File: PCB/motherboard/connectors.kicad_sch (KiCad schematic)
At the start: 9 parts, among them J1 Conn_01x04, J2 Conn_01x08, J3 Conn_01x06, J4 Conn_01x03, J5 Conn_01x03, J6 Conn_01x02, J7 Screw_Terminal_01x03, J8 Screw_Terminal_01x09, J9 Conn_01x11

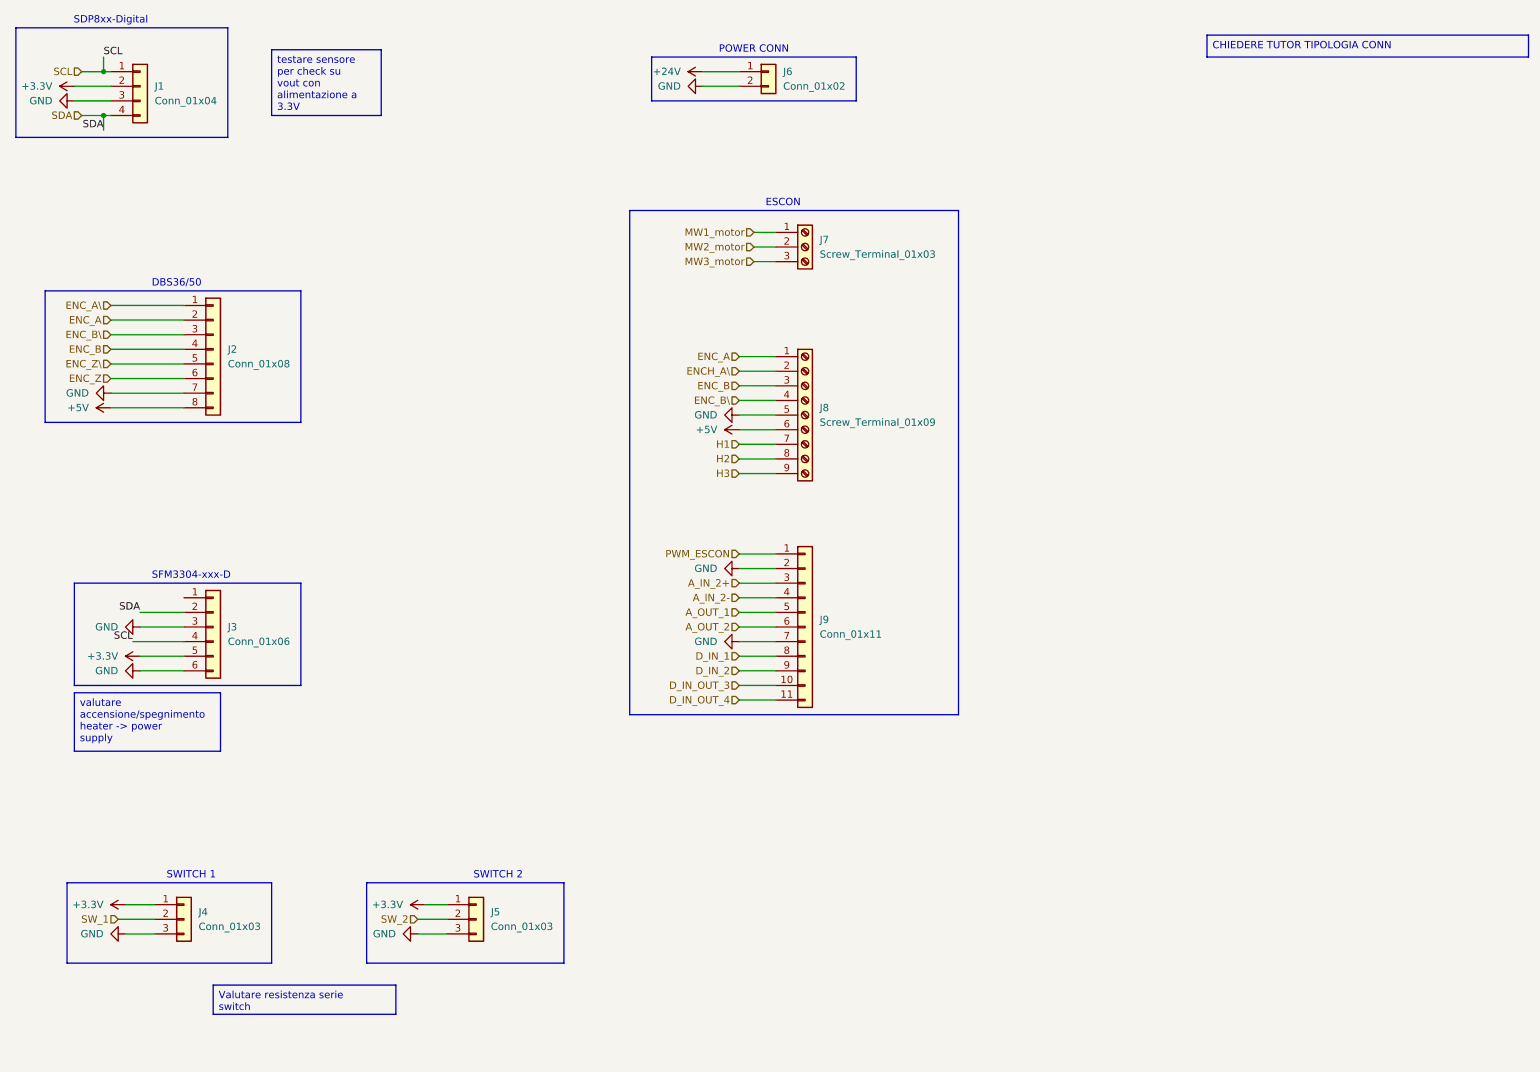
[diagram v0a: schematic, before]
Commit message: reverse current protection on ESCON+others
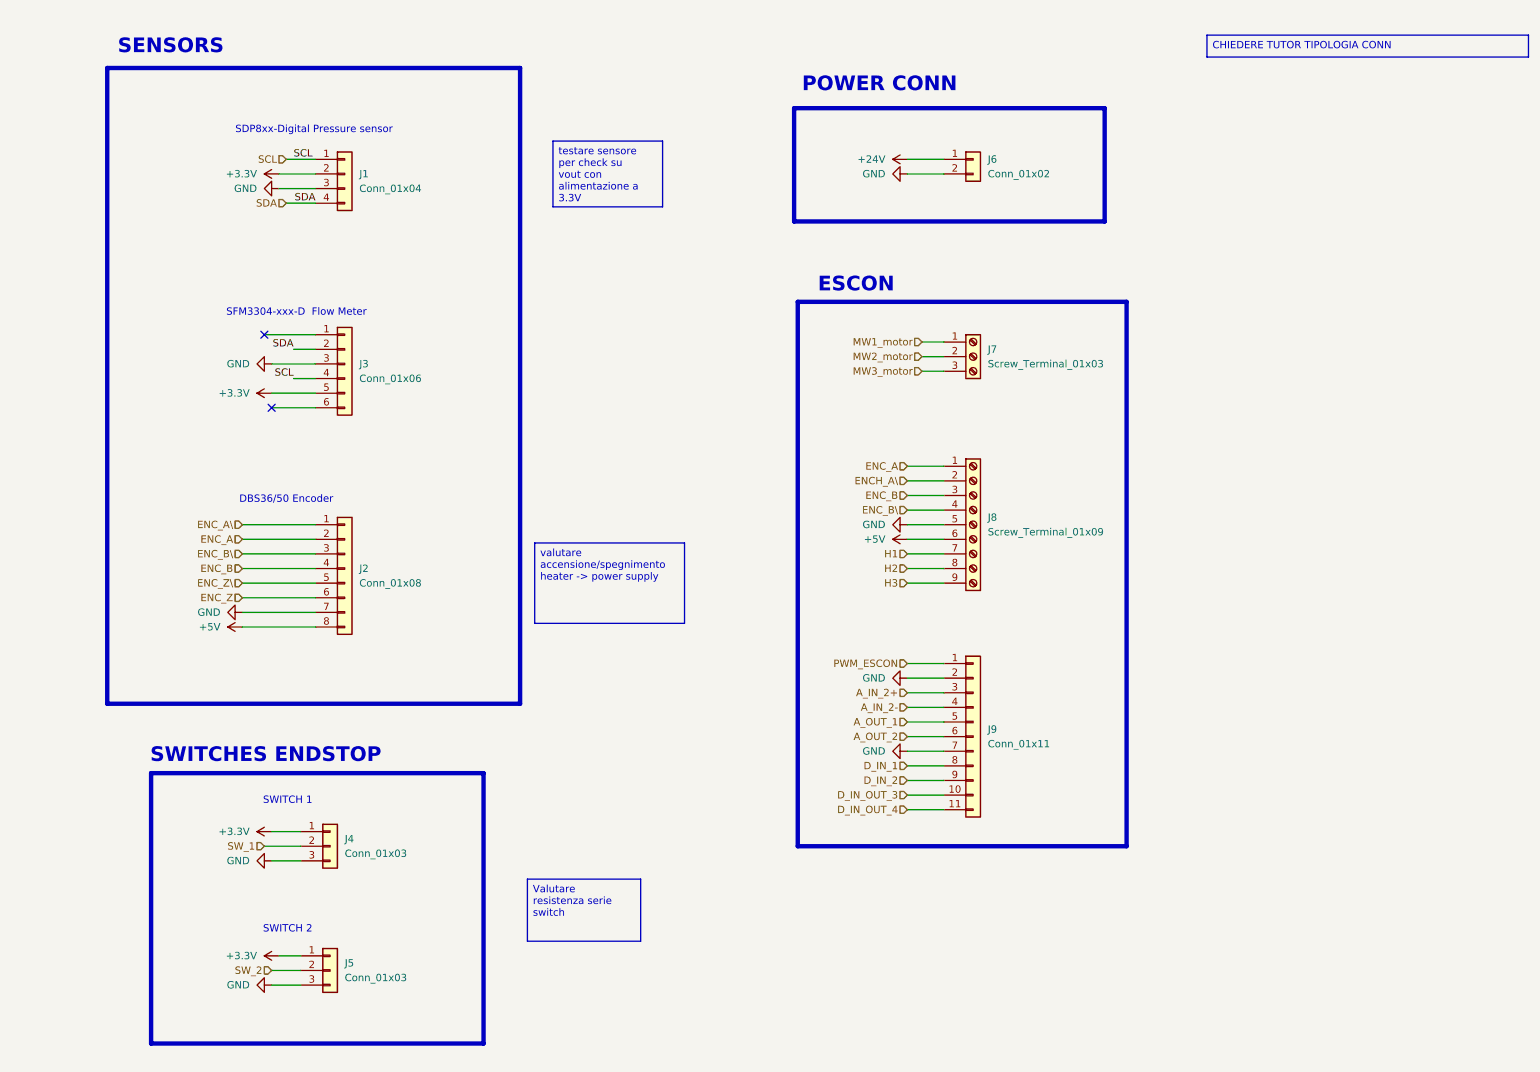
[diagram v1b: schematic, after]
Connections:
- net GND: no longer J3.6 (Pin_6)
- no-connect marks 0 -> 2
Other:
- note added: "DBS36/50 Encoder"
- note added: "SDP8xx-Digital Pressure sensor"
- note added: "SENSORS"
- note added: "SFM3304-xxx-D Flow Meter"
- note added: "SWITCHES ENDSTOP"
- note removed: "DBS36/50"
- note removed: "SDP8xx-Digital"
- note removed: "SFM3304-xxx-D"
- moved on the sheet: J1, J2, J3, J4, J5, J6, J7, J8, J9

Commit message: collegamenti tra blocchi schematico, sistemati connettori,finita la parte di shunt monitor per back EMF escon, aggiunti status LED, aggiunti bulk cap su alimentazione+altre modifiche
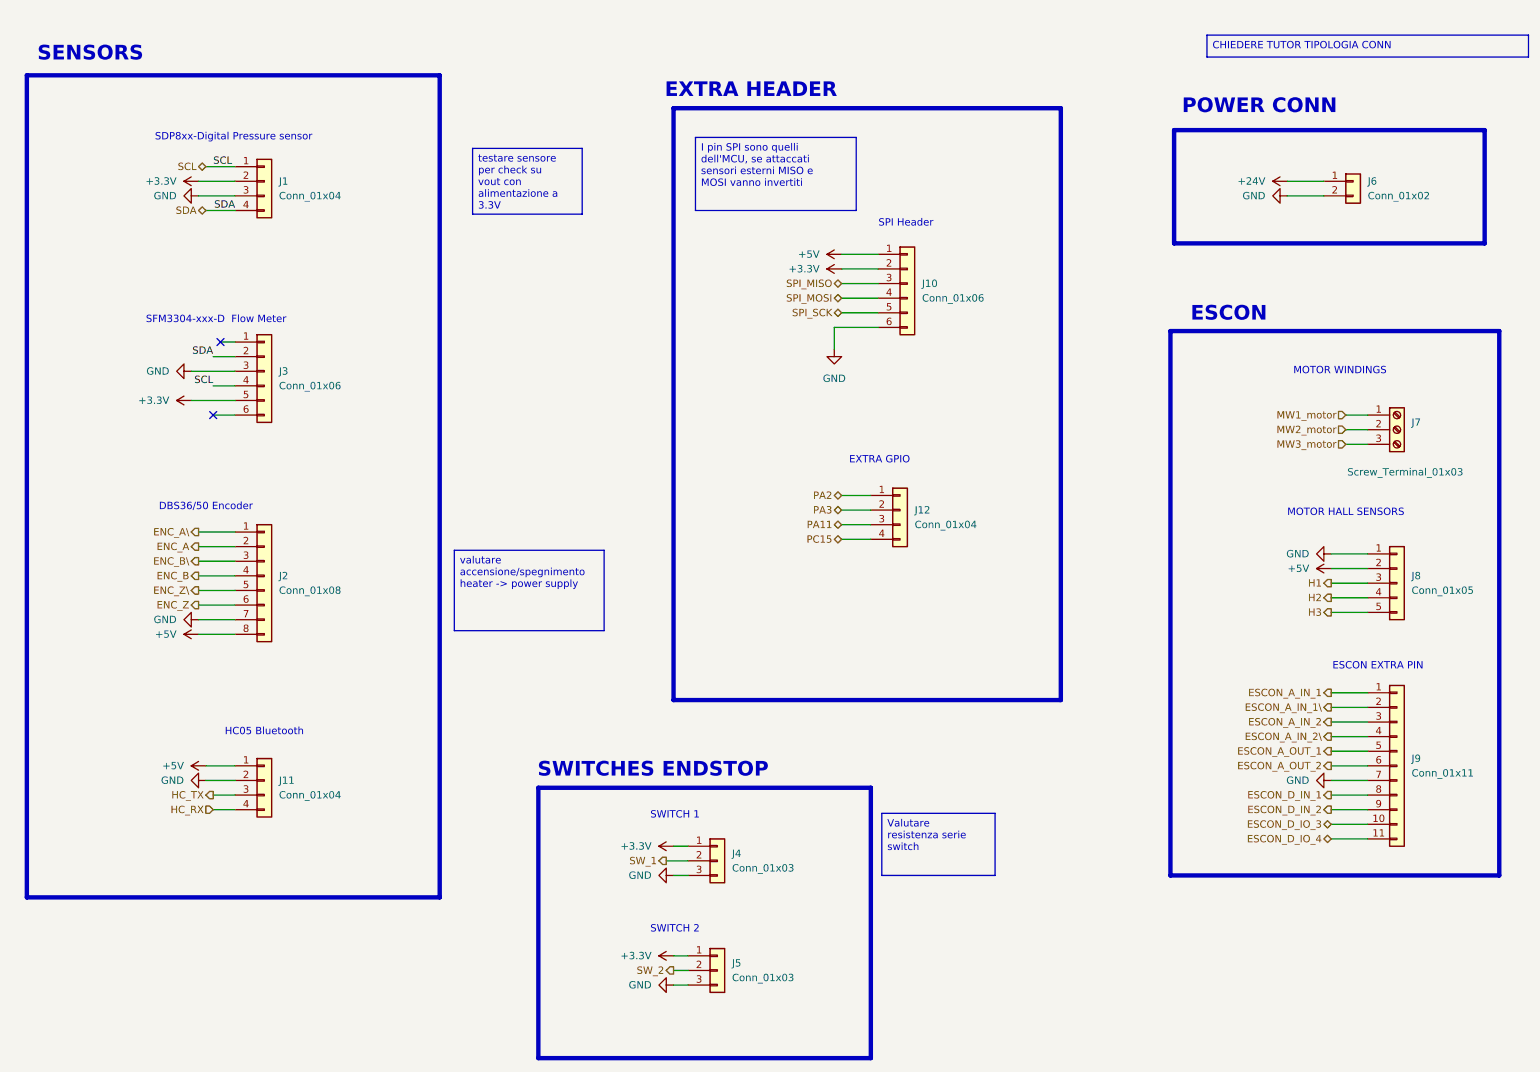
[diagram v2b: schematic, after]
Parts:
- removed J8: Screw_Terminal_01x09, symbol Connector:Screw_Terminal_01x09
- added J10: Conn_01x06, symbol Connector_Generic:Conn_01x06
- added J11, J12: Conn_01x04, symbol Connector_Generic:Conn_01x04
- added J8: Conn_01x05, symbol Connector_Generic:Conn_01x05
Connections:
- net +3.3V: now also J10.2 (Pin_2)
- net +5V: now also J10.1 (Pin_1), J11.1 (Pin_1), J8.2 (Pin_2)
- net GND: now also J10.6 (Pin_6), J11.2 (Pin_2), J8.1 (Pin_1); no longer J9.2 (Pin_2)
- net H1: now also J8.3 (Pin_3)
- net H2: now also J8.4 (Pin_4)
- net H3: now also J8.5 (Pin_5)
- net A_IN_2+ renamed ESCON_A_IN_2
- net A_IN_2- renamed ESCON_A_IN_2\
- net A_OUT_1 renamed ESCON_A_OUT_1
- net A_OUT_2 renamed ESCON_A_OUT_2
- net D_IN_1 renamed ESCON_D_IN_1
- net D_IN_2 renamed ESCON_D_IN_2
- net D_IN_OUT_3 renamed ESCON_D_IO_3
- net D_IN_OUT_4 renamed ESCON_D_IO_4
- net PWM_ESCON renamed ESCON_A_IN_1
- new net ESCON_A_IN_1\: J9.2 (Pin_2)
- new net HC_RX: J11.4 (Pin_4)
- new net HC_TX: J11.3 (Pin_3)
- new net PA11: J12.3 (Pin_3)
- new net PA2: J12.1 (Pin_1)
- new net PA3: J12.2 (Pin_2)
- new net PC15: J12.4 (Pin_4)
- new net SPI_MISO: J10.3 (Pin_3)
- new net SPI_MOSI: J10.4 (Pin_4)
- new net SPI_SCK: J10.5 (Pin_5)
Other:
- note added: "ESCON EXTRA PIN"
- note added: "EXTRA GPIO"
- note added: "EXTRA HEADER"
- note added: "HC05 Bluetooth"
- note added: "MOTOR HALL SENSORS"
- note added: "MOTOR WINDINGS"
- note added: "SPI Header"
- moved on the sheet: J1, J2, J3, J4, J5, J6, J7, J9

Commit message: schematics need only sizing
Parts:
- renumbered J7 to J10, J8 to J11, J9 to J12, J3 to J2, J2 to J3, J11 to J4, J4 to J5, J5 to J6, J12 to J7, J10 to J8, J6 to J9
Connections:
- net HEAT_VDD: now reaches J2.1 (Pin_1)
- net HEAT_GND: now reaches J2.6 (Pin_6)
- no-connect marks 2 -> 0

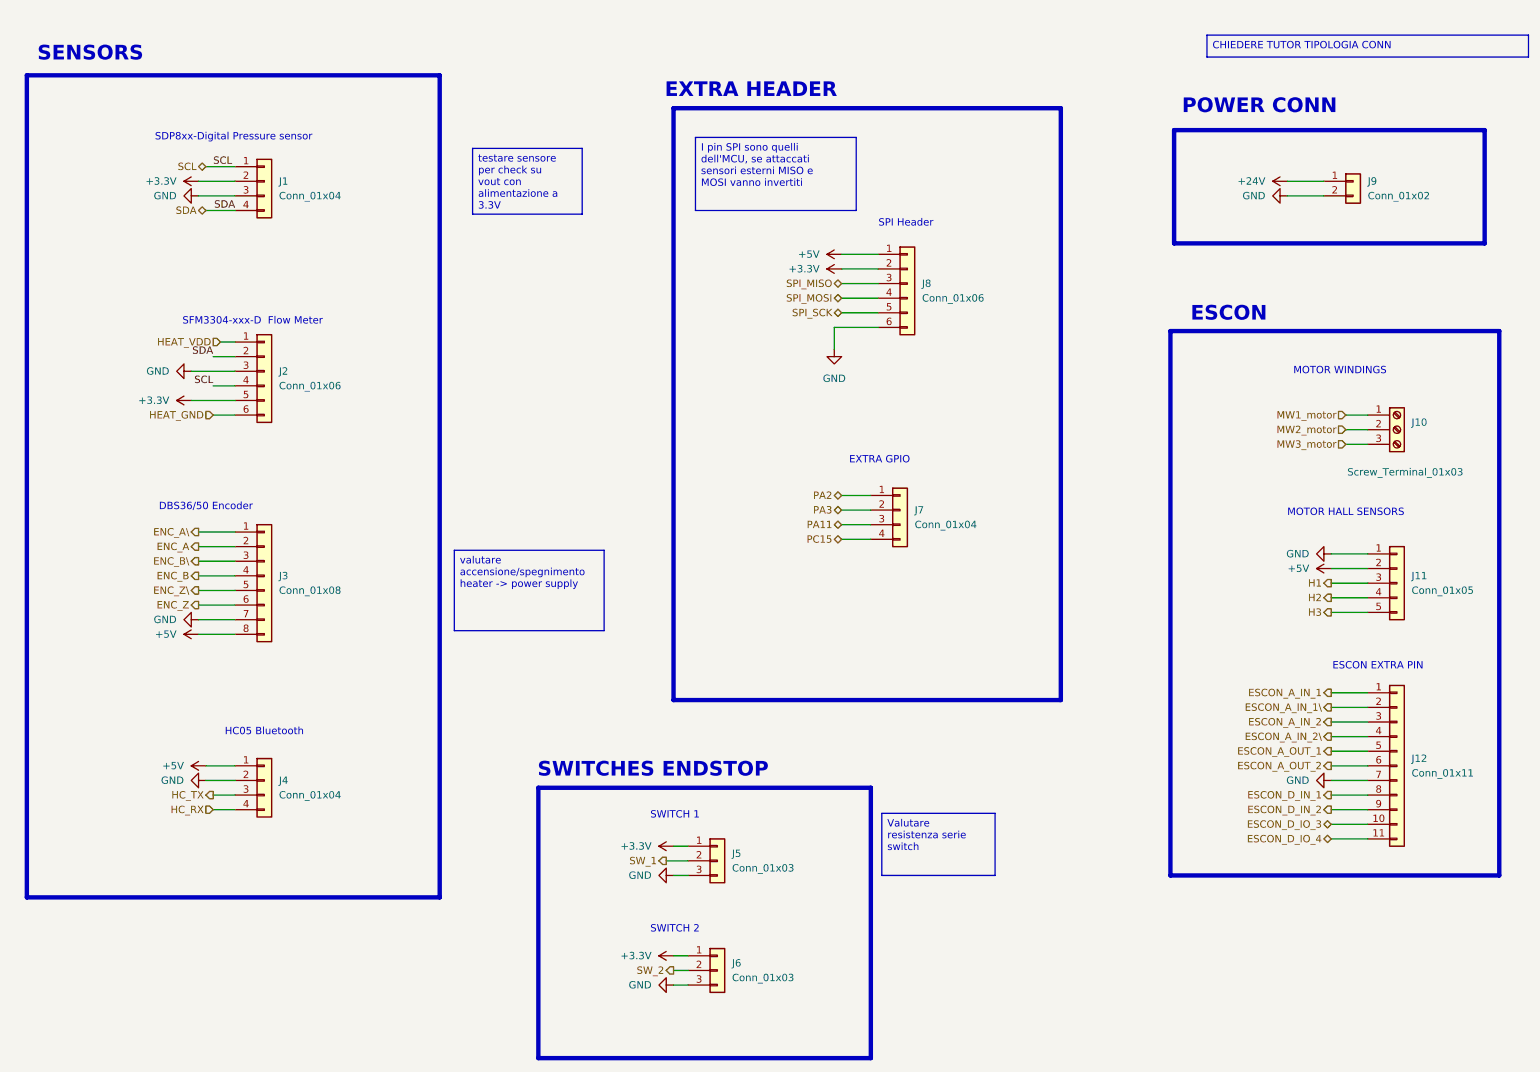
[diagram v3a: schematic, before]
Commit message: sizing schematics done
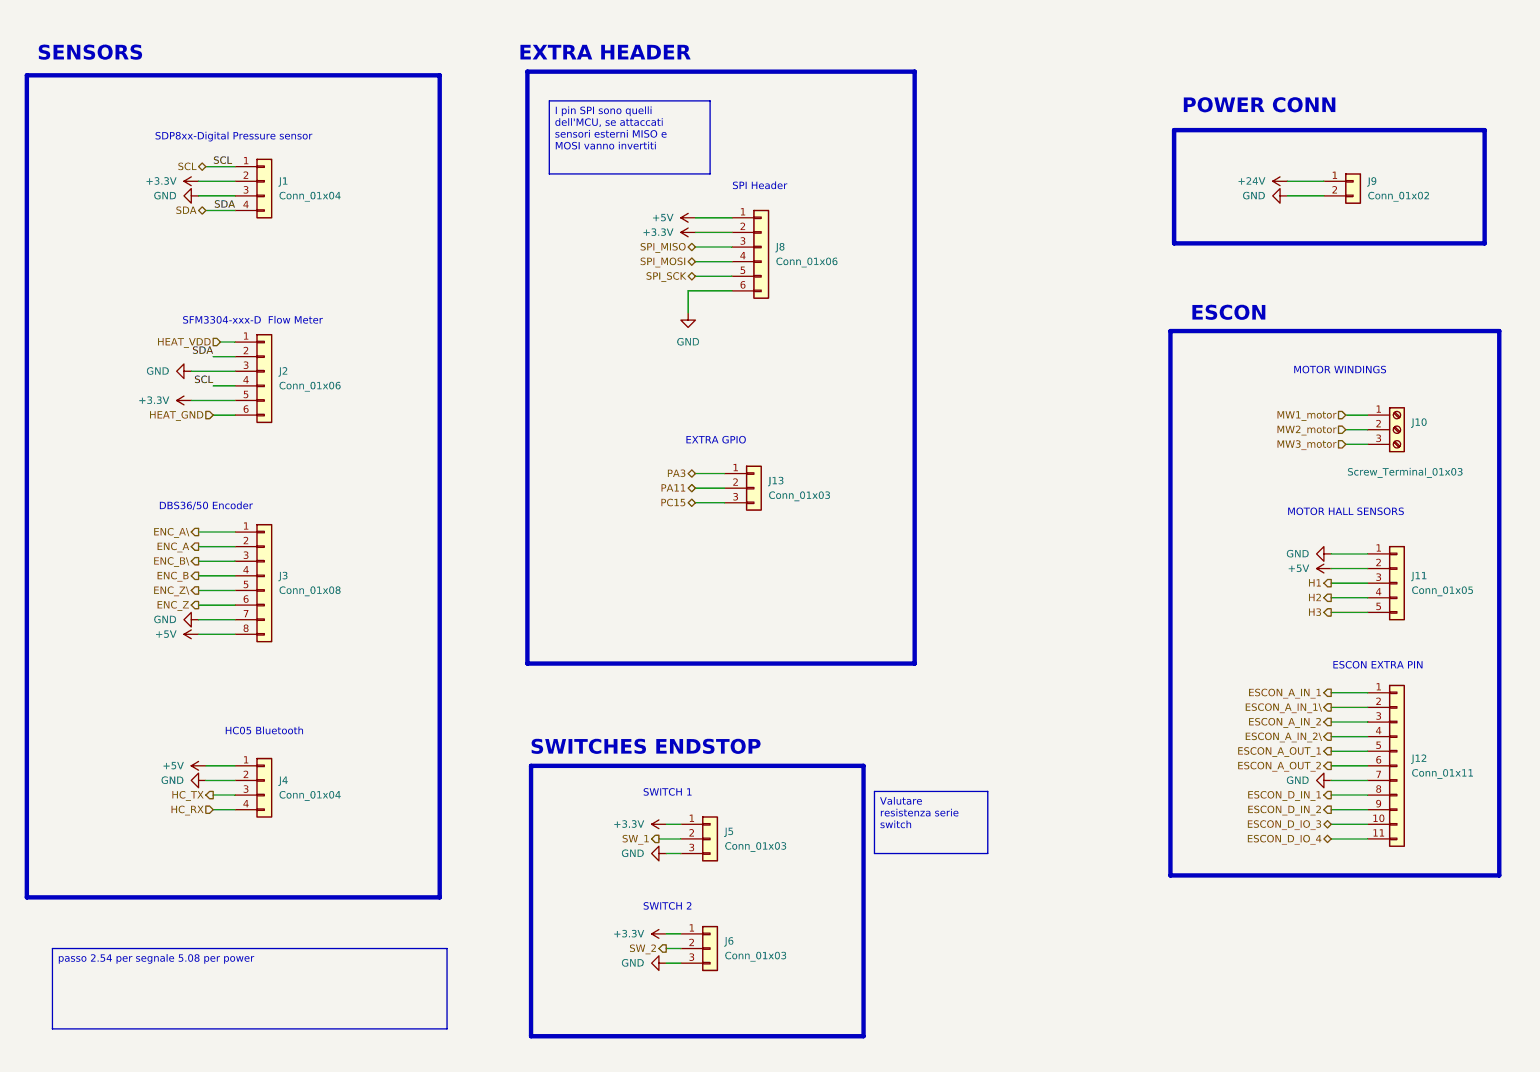
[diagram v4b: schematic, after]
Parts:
- removed J7: Conn_01x04, symbol Connector_Generic:Conn_01x04
- added J13: Conn_01x03, symbol Connector_Generic:Conn_01x03
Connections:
- net PA11: now also J13.2 (Pin_2)
- net PA3: now also J13.1 (Pin_1)
- net PC15: now also J13.3 (Pin_3)
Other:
- moved on the sheet: J5, J6, J8

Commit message: assegnazione footprint connettori
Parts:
- J1, J4: footprint (none) -> TerminalBlock_Phoenix:TerminalBlock_Phoenix_MPT-0,5-4-2.54_1x04_P2.54mm_Horizontal
- J10, J13, J5, J6: footprint (none) -> TerminalBlock_Phoenix:TerminalBlock_Phoenix_MPT-0,5-3-2.54_1x03_P2.54mm_Horizontal
- J11: footprint (none) -> TerminalBlock_Phoenix:TerminalBlock_Phoenix_MPT-0,5-5-2.54_1x05_P2.54mm_Horizontal
- J12: footprint (none) -> TerminalBlock_Phoenix:TerminalBlock_Phoenix_MPT-0,5-11-2.54_1x11_P2.54mm_Horizontal
- J2, J8: footprint (none) -> TerminalBlock_Phoenix:TerminalBlock_Phoenix_MPT-0,5-6-2.54_1x06_P2.54mm_Horizontal
- J3: footprint (none) -> TerminalBlock_Phoenix:TerminalBlock_Phoenix_MPT-0,5-8-2.54_1x08_P2.54mm_Horizontal
- J9: footprint (none) -> TerminalBlock_Phoenix:TerminalBlock_Phoenix_MKDS-3-2-5.08_1x02_P5.08mm_Horizontal
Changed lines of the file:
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@@
 			)
 		)
-		(property "Footprint" ""
+		(property "Footprint" "TerminalBlock_Phoenix:TerminalBlock_Phoenix_MPT-0,5-3-2.54_1x03_P2.54mm_Horizontal"
 			(at 148.59 96.52 0)
 			(hide yes)
@@
 			)
 		)
-		(property "Footprint" ""
+		(property "Footprint" "TerminalBlock_Phoenix:TerminalBlock_Phoenix_MPT-0,5-4-2.54_1x04_P2.54mm_Horizontal"
 			(at 63.5 147.32 0)
 			(hide yes)
@@
 			)
 		)
-		(property "Footprint" ""
+		(property "Footprint" "TerminalBlock_Phoenix:TerminalBlock_Phoenix_MKDS-3-2-5.08_1x02_P5.08mm_Horizontal"
 			(at 252.73 43.18 0)
 			(hide yes)
@@
 			)
 		)
-		(property "Footprint" ""
+		(property "Footprint" "TerminalBlock_Phoenix:TerminalBlock_Phoenix_MPT-0,5-6-2.54_1x06_P2.54mm_Horizontal"
 			(at 63.5 76.2 0)
 			(hide yes)
@@
 			)
 		)
-		(property "Footprint" ""
+		(property "Footprint" "TerminalBlock_Phoenix:TerminalBlock_Phoenix_MPT-0,5-3-2.54_1x03_P2.54mm_Horizontal"
 			(at 260.35 86.36 0)
 			(hide yes)
@@
 			)
 		)
-		(property "Footprint" ""
+		(property "Footprint" "TerminalBlock_Phoenix:TerminalBlock_Phoenix_MPT-0,5-11-2.54_1x11_P2.54mm_Horizontal"
 			(at 260.35 144.78 0)
 			(hide yes)
@@
 			)
 		)
-		(property "Footprint" ""
+		(property "Footprint" "TerminalBlock_Phoenix:TerminalBlock_Phoenix_MPT-0,5-3-2.54_1x03_P2.54mm_Horizontal"
 			(at 140.97 157.48 0)
 			(hide yes)
@@
 			)
 		)
-		(property "Footprint" ""
+		(property "Footprint" "TerminalBlock_Phoenix:TerminalBlock_Phoenix_MPT-0,5-5-2.54_1x05_P2.54mm_Horizontal"
 			(at 260.35 113.03 0)
 			(hide yes)
@@
 			)
 		)
-		(property "Footprint" ""
+		(property "Footprint" "TerminalBlock_Phoenix:TerminalBlock_Phoenix_MPT-0,5-4-2.54_1x04_P2.54mm_Horizontal"
 			(at 63.5 43.18 0)
 			(hide yes)
@@
 			)
 		)
-		(property "Footprint" ""
+		(property "Footprint" "TerminalBlock_Phoenix:TerminalBlock_Phoenix_MPT-0,5-3-2.54_1x03_P2.54mm_Horizontal"
 			(at 140.97 176.53 0)
 			(hide yes)
@@
 			)
 		)
-		(property "Footprint" ""
+		(property "Footprint" "TerminalBlock_Phoenix:TerminalBlock_Phoenix_MPT-0,5-6-2.54_1x06_P2.54mm_Horizontal"
 			(at 149.86 54.61 0)
 			(hide yes)
@@
 			)
 		)
-		(property "Footprint" ""
+		(property "Footprint" "TerminalBlock_Phoenix:TerminalBlock_Phoenix_MPT-0,5-8-2.54_1x08_P2.54mm_Horizontal"
 			(at 63.5 111.76 0)
 			(hide yes)
